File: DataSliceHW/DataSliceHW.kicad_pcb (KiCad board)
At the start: 2 copper layers, 85.5 x 54 mm, 119 parts, among them J1 Micro_SD_Card_Det2, Q1 BC847BDW1, SW1 SKRPABE010, SW10 SKRPABE010, SW11 SKRPABE010, SW12 SKRPABE010, SW13 SKRPABE010, SW14 SKRPABE010, SW15 SKRPABE010, SW16 SKRPABE010, SW17 SKRPABE010, SW18 SKRPABE010, SW19 SKRPABE010, SW2 SKRPABE010, SW20 SKRPABE010, SW21 SKRPABE010, SW22 SKRPABE010, SW23 SKRPABE010, SW24 SKRPABE010, SW25 SKRPABE010, SW26 SKRPABE010, SW27 SKRPABE010, SW28 SKRPABE010, SW29 SKRPABE010, SW3 SKRPABE010, SW30 SKRPABE010, SW31 SKRPABE010, SW32 SKRPABE010, SW33 SKRPABE010, SW34 SKRPABE010, SW35 SKRPABE010, SW36 SKRPABE010, SW37 SKRPABE010, SW38 SKRPABE010, SW39 SKRPABE010, SW4 SKRPABE010, SW40 SKRPABE010, SW41 SKRPABE010, SW42 SKRPABE010, SW43 SKRPABE010, SW44 SKRPABE010, SW45 SKRPABE010, SW46 SKRPABE010, SW47 SKRPABE010, SW48 SKRPABE010, SW49 SKRKAHE020, SW5 SKRPABE010, SW50 SKRKAHE020, SW6 SKRPABE010, SW7 SKRPABE010, SW8 SKRPABE010, SW9 SKRPABE010, U1 ESP32-S3-WROOM-1, U2 CP2102N-Axx-xQFN28

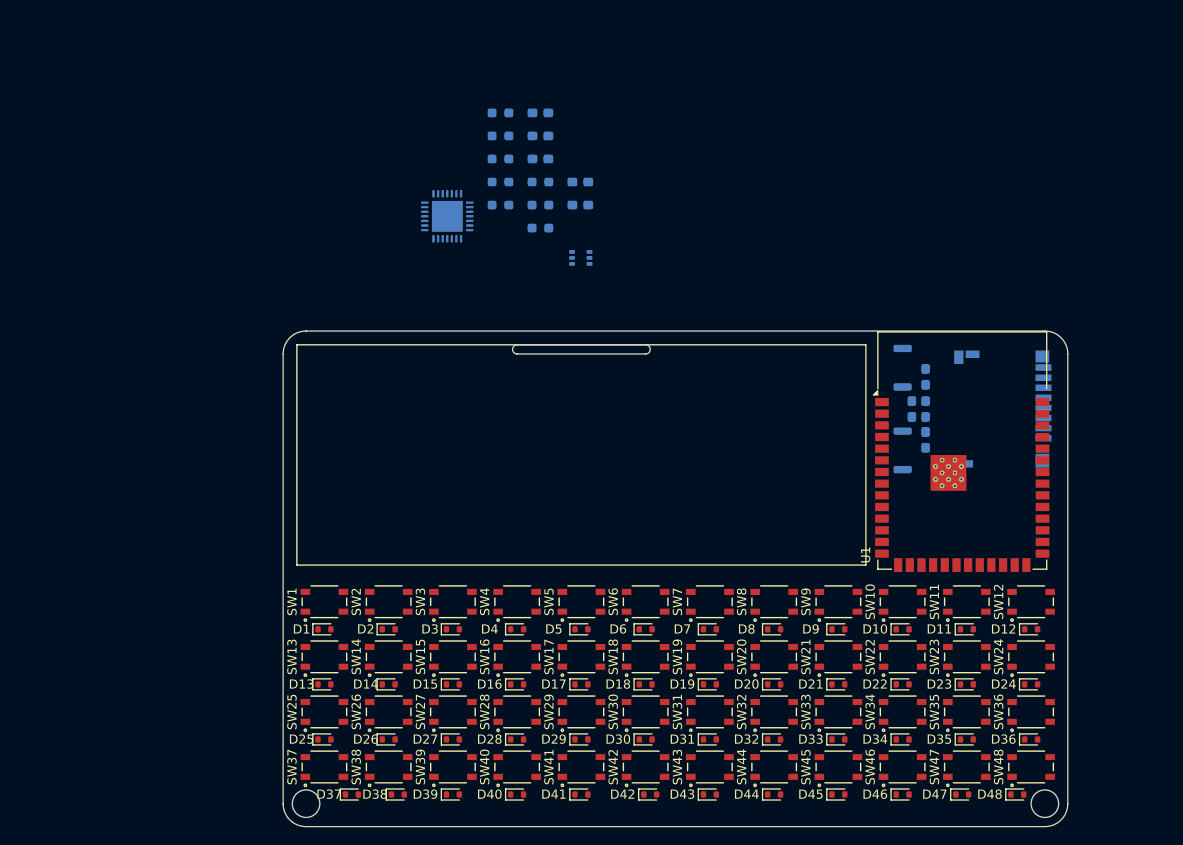
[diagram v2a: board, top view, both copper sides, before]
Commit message: Added OLED schematic
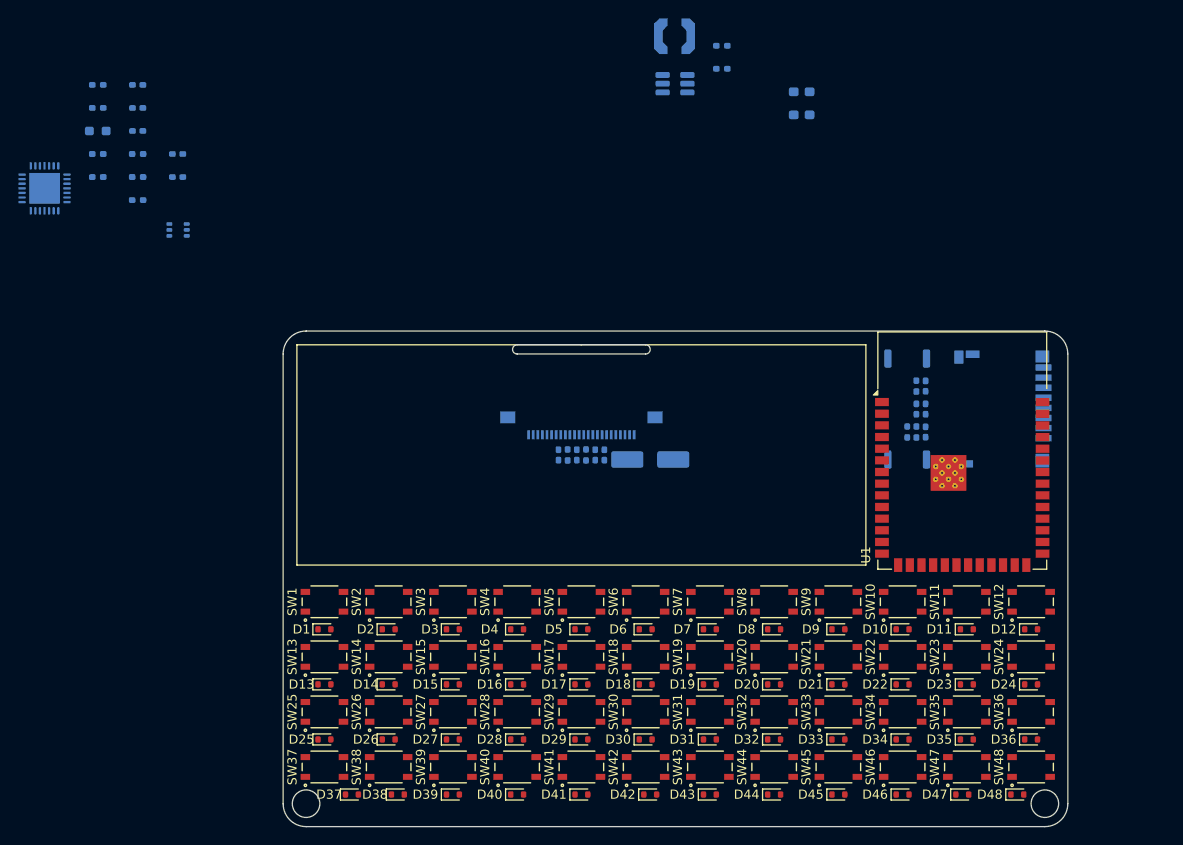
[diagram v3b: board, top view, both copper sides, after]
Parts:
- added C10: 22uF/50V(10%), Capacitor_SMD:C_0603_1608Metric_Pad1.08x0.95mm_HandSolder, B.Cu at (106.5, 23.9)
- added C11: 22uF/50V(10%), Capacitor_SMD:C_0603_1608Metric_Pad1.08x0.95mm_HandSolder, B.Cu at (106.5, 26.4)
- added C12: 4.7uF/50V(10%), Capacitor_SMD:C_0402_1005Metric_Pad0.74x0.62mm_HandSolder, B.Cu at (85.0, 63.5)
- added C5: 4.7uF/16V(10%), Capacitor_SMD:C_0402_1005Metric_Pad0.74x0.62mm_HandSolder, B.Cu at (80.0, 63.5)
- added C8: 100nF/16V(10%), Capacitor_SMD:C_0402_1005Metric_Pad0.74x0.62mm_HandSolder, B.Cu at (82.0, 63.5)
- added C9: 4.7uF/50V(10%), Capacitor_SMD:C_0402_1005Metric_Pad0.74x0.62mm_HandSolder, B.Cu at (84.0, 63.5)
- added D49: SS14, Diode_SMD:D_SMA_Handsoldering, B.Cu at (90.0, 64.0)
- added J2: 6871XX183622_687124183622, DataSlice:687124183622, B.Cu at (82.5, 59.0)
- added L1: 4.7uH, Inductor_SMD:L_Coilcraft_LPS4018, B.Cu at (92.7, 17.9)
- added R10: 200K(1%), Resistor_SMD:R_0402_1005Metric_Pad0.72x0.64mm_HandSolder, B.Cu at (97.8, 18.9)
- added R11: 10K(1%), Resistor_SMD:R_0402_1005Metric_Pad0.72x0.64mm_HandSolder, B.Cu at (97.8, 21.4)
- added R2: 10K(1%), Resistor_SMD:R_0402_1005Metric_Pad0.72x0.64mm_HandSolder, B.Cu at (119.0, 56.0)
- added R4: 10K(1%), Resistor_SMD:R_0402_1005Metric_Pad0.72x0.64mm_HandSolder, B.Cu at (81.0, 63.5)
- added R7: 4.7K(1%), Resistor_SMD:R_0402_1005Metric_Pad0.72x0.64mm_HandSolder, B.Cu at (119.0, 61.0)
- added R8: 4.7K(1%), Resistor_SMD:R_0402_1005Metric_Pad0.72x0.64mm_HandSolder, B.Cu at (118.0, 61.0)
- added R9: 1M(1%), Resistor_SMD:R_0402_1005Metric_Pad0.72x0.64mm_HandSolder, B.Cu at (83.0, 63.5)
- added U3: MT3608/SX1308, Package_TO_SOT_SMD:SOT-23-6_Handsoldering, B.Cu at (92.7, 23.1)
- C1, C2: footprint Capacitor_SMD:C_0603_1608Metric_Pad1.08x0.95mm_HandSolder -> Capacitor_SMD:C_0402_1005Metric_Pad0.74x0.62mm_HandSolder
- C13: renamed from C5; footprint Capacitor_SMD:C_0603_1608Metric_Pad1.08x0.95mm_HandSolder -> Capacitor_SMD:C_0402_1005Metric_Pad0.74x0.62mm_HandSolder
- C14: renamed from C6; footprint Capacitor_SMD:C_0603_1608Metric_Pad1.08x0.95mm_HandSolder -> Capacitor_SMD:C_0402_1005Metric_Pad0.74x0.62mm_HandSolder
- C15: renamed from C9; footprint Capacitor_SMD:C_0603_1608Metric_Pad1.08x0.95mm_HandSolder -> Capacitor_SMD:C_0402_1005Metric_Pad0.74x0.62mm_HandSolder
- C3: renamed from C7; footprint Capacitor_SMD:C_0603_1608Metric_Pad1.08x0.95mm_HandSolder -> Capacitor_SMD:C_0402_1005Metric_Pad0.74x0.62mm_HandSolder
- C4: renamed from C8; footprint Capacitor_SMD:C_0603_1608Metric_Pad1.08x0.95mm_HandSolder -> Capacitor_SMD:C_0402_1005Metric_Pad0.74x0.62mm_HandSolder
- C6: renamed from C3; footprint Capacitor_SMD:C_0603_1608Metric_Pad1.08x0.95mm_HandSolder -> Capacitor_SMD:C_0402_1005Metric_Pad0.74x0.62mm_HandSolder
- C7: renamed from C4; footprint Capacitor_SMD:C_0603_1608Metric_Pad1.08x0.95mm_HandSolder -> Capacitor_SMD:C_0402_1005Metric_Pad0.74x0.62mm_HandSolder
- R1: footprint Resistor_SMD:R_0603_1608Metric_Pad0.98x0.95mm_HandSolder -> Resistor_SMD:R_0402_1005Metric_Pad0.72x0.64mm_HandSolder
- R12: renamed from R4; footprint Resistor_SMD:R_0603_1608Metric_Pad0.98x0.95mm_HandSolder -> Resistor_SMD:R_0402_1005Metric_Pad0.72x0.64mm_HandSolder
- R13: renamed from R5; footprint Resistor_SMD:R_0603_1608Metric_Pad0.98x0.95mm_HandSolder -> Resistor_SMD:R_0402_1005Metric_Pad0.72x0.64mm_HandSolder
- R14: renamed from R7; footprint Resistor_SMD:R_0603_1608Metric_Pad0.98x0.95mm_HandSolder -> Resistor_SMD:R_0402_1005Metric_Pad0.72x0.64mm_HandSolder
- R15: renamed from R8; footprint Resistor_SMD:R_0603_1608Metric_Pad0.98x0.95mm_HandSolder -> Resistor_SMD:R_0402_1005Metric_Pad0.72x0.64mm_HandSolder
- R3: renamed from R2; footprint Resistor_SMD:R_0603_1608Metric_Pad0.98x0.95mm_HandSolder -> Resistor_SMD:R_0402_1005Metric_Pad0.72x0.64mm_HandSolder
- R5: renamed from R3; footprint Resistor_SMD:R_0603_1608Metric_Pad0.98x0.95mm_HandSolder -> Resistor_SMD:R_0402_1005Metric_Pad0.72x0.64mm_HandSolder
- moved C13 44.0 mm to (38.5, 33.2)
- moved C7 44.0 mm to (38.5, 30.7)
- moved Q1 44.0 mm to (38.5, 39.0)
- moved R12 44.0 mm to (29.8, 23.2)
- moved R13 44.0 mm to (29.8, 25.7)
- moved R14 44.0 mm to (29.8, 30.7)
- moved R15 44.0 mm to (29.8, 33.2)
- moved R6 44.0 mm to (29.8, 28.2)
- moved U2 44.0 mm to (24.0, 34.5)
- moved C15 44.0 mm to (34.1, 28.2)
- moved C3 44.0 mm to (34.1, 23.2)
- moved C4 44.0 mm to (34.1, 25.7)
- moved R1 44.0 mm to (34.1, 30.7)
- moved R3 44.0 mm to (34.1, 33.2)
- moved R5 44.0 mm to (34.1, 35.7)
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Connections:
- J1 pad 1: /SD_D2 -> unconnected-(J1-DAT2-Pad1)
- J1 pad 2: /SD_D3 -> Net-(J1-DAT3/CD)
- J1 pad 8: /SD_D1 -> unconnected-(J1-DAT1-Pad8)
- U1 pad 33: /SD_D1 -> unconnected-(U1-IO40-Pad33)
- U1 pad 34: /SD_D2 -> /I2C_SDA
- U1 pad 35: /SD_D3 -> /I2C_SCL

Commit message: Schematic and board progress
Updated gitignore and removed some ignored files
Added power schematic with battery chagrer
Some adjustments to components
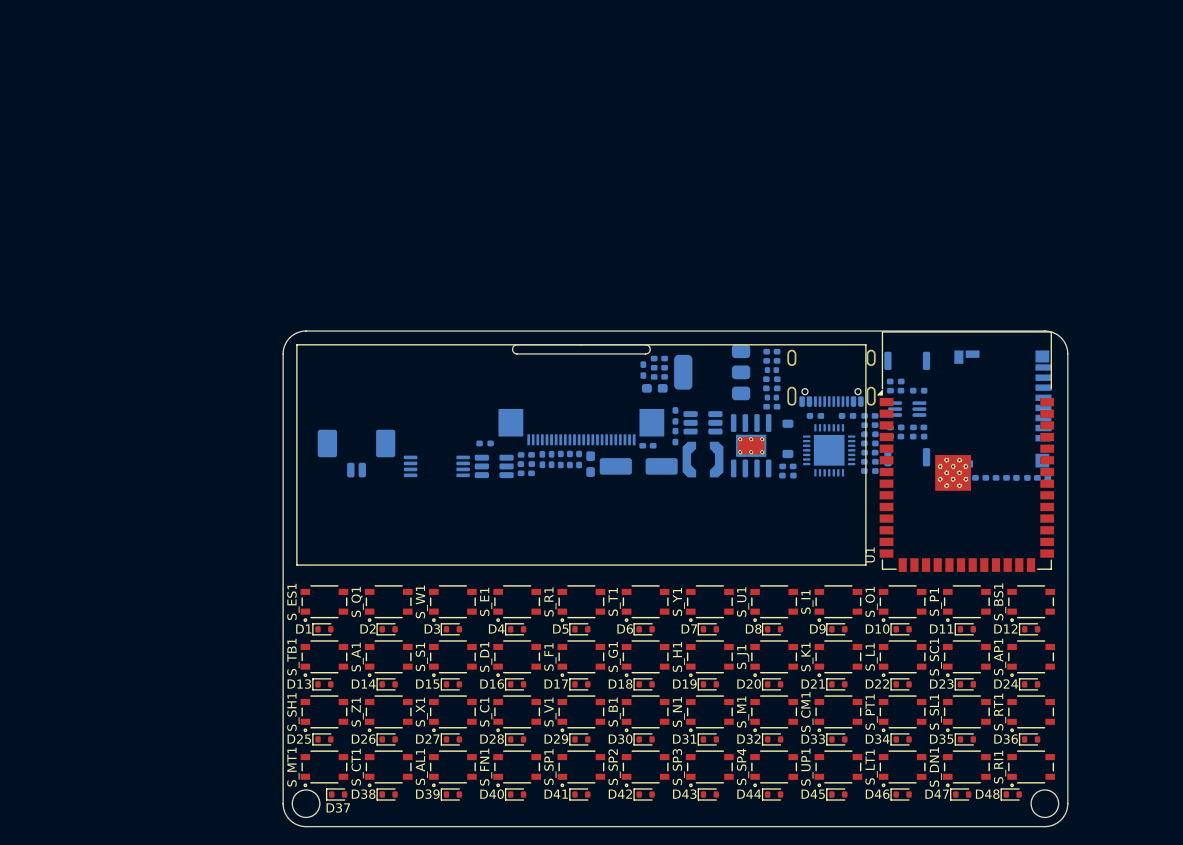
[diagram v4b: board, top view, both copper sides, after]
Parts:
- removed SW1, SW10, SW11, SW12, SW13, SW14, SW15, SW16, SW17, SW18, SW19, SW2, SW20, SW21, SW22, SW23, SW24, SW25, SW26, SW27, SW28, SW29, SW3, SW30, SW31, SW32, SW33, SW34, SW35, SW36, SW37, SW38, SW39, SW4, SW40, SW41, SW42, SW43, SW44, SW45, SW46, SW47, SW48, SW5, SW6, SW7, SW8, SW9: SKRPABE010, DataSlice:SW4_SKRPABE010_ALPS
- added C10: 10uF/25V(20%), Capacitor_SMD:C_0402_1005Metric_Pad0.74x0.62mm_HandSolder, B.Cu at (103.2, 53.2)
- added C11: 0.1uF/50V(10%), Capacitor_SMD:C_0402_1005Metric_Pad0.74x0.62mm_HandSolder, B.Cu at (103.2, 52.2)
- added C12: 0.1uF/50V(10%), Capacitor_SMD:C_0402_1005Metric_Pad0.74x0.62mm_HandSolder, B.Cu at (91.0, 55.0)
- added C13: 10uF/25V(20%), Capacitor_SMD:C_0402_1005Metric_Pad0.74x0.62mm_HandSolder, B.Cu at (91.0, 54.0)
- added C15: 10uF/25V(20%), Capacitor_SMD:C_0402_1005Metric_Pad0.74x0.62mm_HandSolder, B.Cu at (76.5, 63.5)
- added C17: 0.1uF/50V(10%), Capacitor_SMD:C_0402_1005Metric_Pad0.74x0.62mm_HandSolder, B.Cu at (76.5, 65.5)
- added C18: 0.1uF/50V(10%), Capacitor_SMD:C_0402_1005Metric_Pad0.74x0.62mm_HandSolder, B.Cu at (103.2, 58.2)
- added C4: 10uF/25V(20%), Capacitor_SMD:C_0402_1005Metric_Pad0.74x0.62mm_HandSolder, B.Cu at (105.0, 64.8)
- added D49: 1N5819HW-7-F, Diode_SMD:D_SOD-123, B.Cu at (105.0, 61.8)
- added D50: RED, LED_SMD:LED_0402_1005Metric, B.Cu at (103.2, 54.2)
- added D51: RED, LED_SMD:LED_0402_1005Metric, B.Cu at (103.2, 57.2)
- added J1: USB4105-GF-A, Connector_USB:USB_C_Receptacle_GCT_USB4105-xx-A_16P_TopMnt_Horizontal, B.Cu at (109.8, 54.0)
- added J4: 53261-0271, Connector_Molex:Molex_PicoBlade_53261-0271_1x02-1MP_P1.25mm_Horizontal, B.Cu at (58.0, 62.8)
- added Q2: FS8205A, Package_SO:TSSOP-8_4.4x3mm_P0.65mm, B.Cu at (66.8, 64.8)
- added R14: 100R(1%), Resistor_SMD:R_0402_1005Metric_Pad0.72x0.64mm_HandSolder, B.Cu at (76.5, 64.5)
- added R15: 1K(1%), Resistor_SMD:R_0402_1005Metric_Pad0.72x0.64mm_HandSolder, B.Cu at (103.2, 56.2)
- added R16: 1K(1%), Resistor_SMD:R_0402_1005Metric_Pad0.72x0.64mm_HandSolder, B.Cu at (72.0, 62.2)
- added R17: 1K(1%), Resistor_SMD:R_0402_1005Metric_Pad0.72x0.64mm_HandSolder, B.Cu at (103.2, 55.2)
- added R18: 3K(1%), Resistor_SMD:R_0402_1005Metric_Pad0.72x0.64mm_HandSolder, B.Cu at (105.0, 65.8)
- added R5: 5.1K(1%), Resistor_SMD:R_0402_1005Metric_Pad0.72x0.64mm_HandSolder, B.Cu at (108.0, 59.2)
- added R6: 5.1K(1%), Resistor_SMD:R_0402_1005Metric_Pad0.72x0.64mm_HandSolder, B.Cu at (111.5, 59.2)
- added S_A1: SKRPABE010, DataSlice:SW4_SKRPABE010_ALPS, F.Cu at (61.5, 85.5)
- added S_AL1: SKRPABE010, DataSlice:SW4_SKRPABE010_ALPS, F.Cu at (68.5, 97.5)
- added S_AP1: SKRPABE010, DataSlice:SW4_SKRPABE010_ALPS, F.Cu at (131.5, 85.5)
- added S_B1: SKRPABE010, DataSlice:SW4_SKRPABE010_ALPS, F.Cu at (89.5, 91.5)
- added S_BS1: SKRPABE010, DataSlice:SW4_SKRPABE010_ALPS, F.Cu at (131.5, 79.5)
- added S_C1: SKRPABE010, DataSlice:SW4_SKRPABE010_ALPS, F.Cu at (75.5, 91.5)
- added S_CM1: SKRPABE010, DataSlice:SW4_SKRPABE010_ALPS, F.Cu at (110.5, 91.5)
- added S_CT1: SKRPABE010, DataSlice:SW4_SKRPABE010_ALPS, F.Cu at (61.5, 97.5)
- added S_D1: SKRPABE010, DataSlice:SW4_SKRPABE010_ALPS, F.Cu at (75.5, 85.5)
- added S_DN1: SKRPABE010, DataSlice:SW4_SKRPABE010_ALPS, F.Cu at (124.5, 97.5)
- added S_E1: SKRPABE010, DataSlice:SW4_SKRPABE010_ALPS, F.Cu at (75.5, 79.5)
- added S_ES1: SKRPABE010, DataSlice:SW4_SKRPABE010_ALPS, F.Cu at (54.5, 79.5)
- added S_F1: SKRPABE010, DataSlice:SW4_SKRPABE010_ALPS, F.Cu at (82.5, 85.5)
- added S_FN1: SKRPABE010, DataSlice:SW4_SKRPABE010_ALPS, F.Cu at (75.5, 97.5)
- added S_G1: SKRPABE010, DataSlice:SW4_SKRPABE010_ALPS, F.Cu at (89.5, 85.5)
- added S_H1: SKRPABE010, DataSlice:SW4_SKRPABE010_ALPS, F.Cu at (96.5, 85.5)
- added S_I1: SKRPABE010, DataSlice:SW4_SKRPABE010_ALPS, F.Cu at (110.5, 79.5)
- added S_J1: SKRPABE010, DataSlice:SW4_SKRPABE010_ALPS, F.Cu at (103.5, 85.5)
- added S_K1: SKRPABE010, DataSlice:SW4_SKRPABE010_ALPS, F.Cu at (110.5, 85.5)
- added S_L1: SKRPABE010, DataSlice:SW4_SKRPABE010_ALPS, F.Cu at (117.5, 85.5)
- added S_LT1: SKRPABE010, DataSlice:SW4_SKRPABE010_ALPS, F.Cu at (117.5, 97.5)
- added S_M1: SKRPABE010, DataSlice:SW4_SKRPABE010_ALPS, F.Cu at (103.5, 91.5)
- added S_MT1: SKRPABE010, DataSlice:SW4_SKRPABE010_ALPS, F.Cu at (54.5, 97.5)
- added S_N1: SKRPABE010, DataSlice:SW4_SKRPABE010_ALPS, F.Cu at (96.5, 91.5)
- added S_O1: SKRPABE010, DataSlice:SW4_SKRPABE010_ALPS, F.Cu at (117.5, 79.5)
- added S_P1: SKRPABE010, DataSlice:SW4_SKRPABE010_ALPS, F.Cu at (124.5, 79.5)
- added S_PT1: SKRPABE010, DataSlice:SW4_SKRPABE010_ALPS, F.Cu at (117.5, 91.5)
- added S_Q1: SKRPABE010, DataSlice:SW4_SKRPABE010_ALPS, F.Cu at (61.5, 79.5)
- added S_R1: SKRPABE010, DataSlice:SW4_SKRPABE010_ALPS, F.Cu at (82.5, 79.5)
- added S_RI1: SKRPABE010, DataSlice:SW4_SKRPABE010_ALPS, F.Cu at (131.5, 97.5)
- added S_RT1: SKRPABE010, DataSlice:SW4_SKRPABE010_ALPS, F.Cu at (131.5, 91.5)
- added S_S1: SKRPABE010, DataSlice:SW4_SKRPABE010_ALPS, F.Cu at (68.5, 85.5)
- added S_SC1: SKRPABE010, DataSlice:SW4_SKRPABE010_ALPS, F.Cu at (124.5, 85.5)
- added S_SH1: SKRPABE010, DataSlice:SW4_SKRPABE010_ALPS, F.Cu at (54.5, 91.5)
- added S_SL1: SKRPABE010, DataSlice:SW4_SKRPABE010_ALPS, F.Cu at (124.5, 91.5)
- added S_SP1: SKRPABE010, DataSlice:SW4_SKRPABE010_ALPS, F.Cu at (82.5, 97.5)
- added S_SP2: SKRPABE010, DataSlice:SW4_SKRPABE010_ALPS, F.Cu at (89.5, 97.5)
- added S_SP3: SKRPABE010, DataSlice:SW4_SKRPABE010_ALPS, F.Cu at (96.5, 97.5)
- added S_SP4: SKRPABE010, DataSlice:SW4_SKRPABE010_ALPS, F.Cu at (103.5, 97.5)
- added S_T1: SKRPABE010, DataSlice:SW4_SKRPABE010_ALPS, F.Cu at (89.5, 79.5)
- added S_TB1: SKRPABE010, DataSlice:SW4_SKRPABE010_ALPS, F.Cu at (54.5, 85.5)
- added S_U1: SKRPABE010, DataSlice:SW4_SKRPABE010_ALPS, F.Cu at (103.5, 79.5)
- added S_UP1: SKRPABE010, DataSlice:SW4_SKRPABE010_ALPS, F.Cu at (110.5, 97.5)
- added S_V1: SKRPABE010, DataSlice:SW4_SKRPABE010_ALPS, F.Cu at (82.5, 91.5)
- added S_W1: SKRPABE010, DataSlice:SW4_SKRPABE010_ALPS, F.Cu at (68.5, 79.5)
- added S_X1: SKRPABE010, DataSlice:SW4_SKRPABE010_ALPS, F.Cu at (68.5, 91.5)
- added S_Y1: SKRPABE010, DataSlice:SW4_SKRPABE010_ALPS, F.Cu at (96.5, 79.5)
- added S_Z1: SKRPABE010, DataSlice:SW4_SKRPABE010_ALPS, F.Cu at (61.5, 91.5)
- added U3: AMS1117-3.3 / SGM2212-3.3, Package_TO_SOT_SMD:SOT-223-3_TabPin2, B.Cu at (96.8, 54.5)
- added U4: DW01A, Package_TO_SOT_SMD:SOT-23-6_Handsoldering, B.Cu at (73.0, 64.8)
- added U5: TP4056-42-ESOP8, Package_SO:SOIC-8-1EP_3.9x4.9mm_P1.27mm_EP2.41x3.3mm_ThermalVias, B.Cu at (101.0, 62.5)
- C16: renamed from C8; value 100nF/16V(10%) -> 0.1uF/50V(10%)
- C2: renamed from C1; value 10uF/16V(10%) -> 10uF/25V(20%)
- C21: renamed from C6; value 100nF/16V(10%) -> 0.1uF/50V(10%)
- C3: value 10uF/16V(10%) -> 10uF/25V(20%)
- C6: renamed from C2; value 100nF/16V(10%) -> 0.1uF/50V(10%)
- C9: renamed from C4; value 100nF/16V(10%) -> 0.1uF/50V(10%)
- J2: value 6871XX183622_687124183622 -> 68712414522; footprint DataSlice:687124183622 -> DataSlice:68712414522
- J3: renamed from J1; value Micro_SD_Card_Det2 -> DM3D-SF
- Q1: footprint Package_TO_SOT_SMD:SOT-363_SC-70-6 -> Package_TO_SOT_SMD:SOT-363_SC-70-6_Handsoldering
- R10: renamed from R6; footprint Resistor_SMD:R_0603_1608Metric_Pad0.98x0.95mm_HandSolder -> Resistor_SMD:R_0402_1005Metric_Pad0.72x0.64mm_HandSolder
- U2: value CP2102N-Axx-xQFN28 -> CP2102N-A02-GQFN28
- moved R2 96.4 mm to (119.2, 61.5)
- moved R1 92.8 mm to (116.8, 55.5), turned to 0 degrees
- moved R7 92.4 mm to (119.2, 56.5), turned to 0 degrees
- moved R10 91.9 mm to (113.9, 65.2), turned to 0 degrees
- moved R3 91.9 mm to (116.8, 60.5)
- moved C7 91.0 mm to (119.2, 60.5), turned to 0 degrees
- moved U2 90.1 mm to (109.5, 63.0), turned to -90 degrees
- moved C3 88.0 mm to (113.9, 60.2)
- moved C9 86.6 mm to (113.9, 59.2), turned to 0 degrees
- moved R4 86.5 mm to (113.9, 64.2)
- moved R8 84.6 mm to (113.9, 61.2)
- moved R9 84.1 mm to (113.9, 62.2), turned to 0 degrees
- moved C8 82.2 mm to (113.9, 63.2), turned to 0 degrees
- moved Q1 81.8 mm to (118.0, 58.5)
- moved C1 81.6 mm to (116.8, 56.5)
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- renumbered C13 to C1, C5 to C14, C9 to C19, C12 to C20, C10 to C22, C11 to C23, C14 to C5, C15 to C7, C7 to C8, D49 to D52, R12 to R1, R7 to R11, R8 to R12, R4 to R13, R9 to R19, R13 to R2, R2 to R20, R10 to R21, R11 to R22, R14 to R3, R1 to R4, R15 to R7, R3 to R8, R5 to R9, SW49 to S_PR1, SW50 to S_RS1, U3 to U6

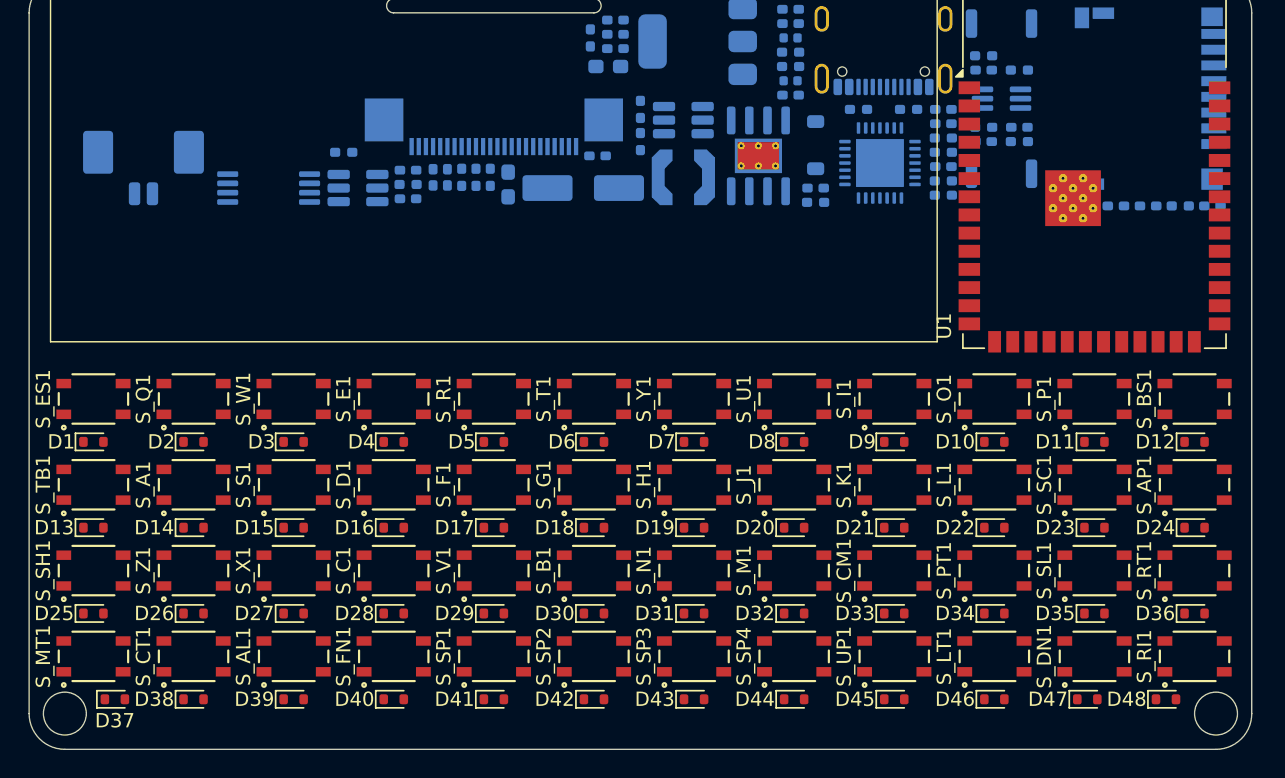
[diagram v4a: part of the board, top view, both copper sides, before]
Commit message: Board adjustments and some renders
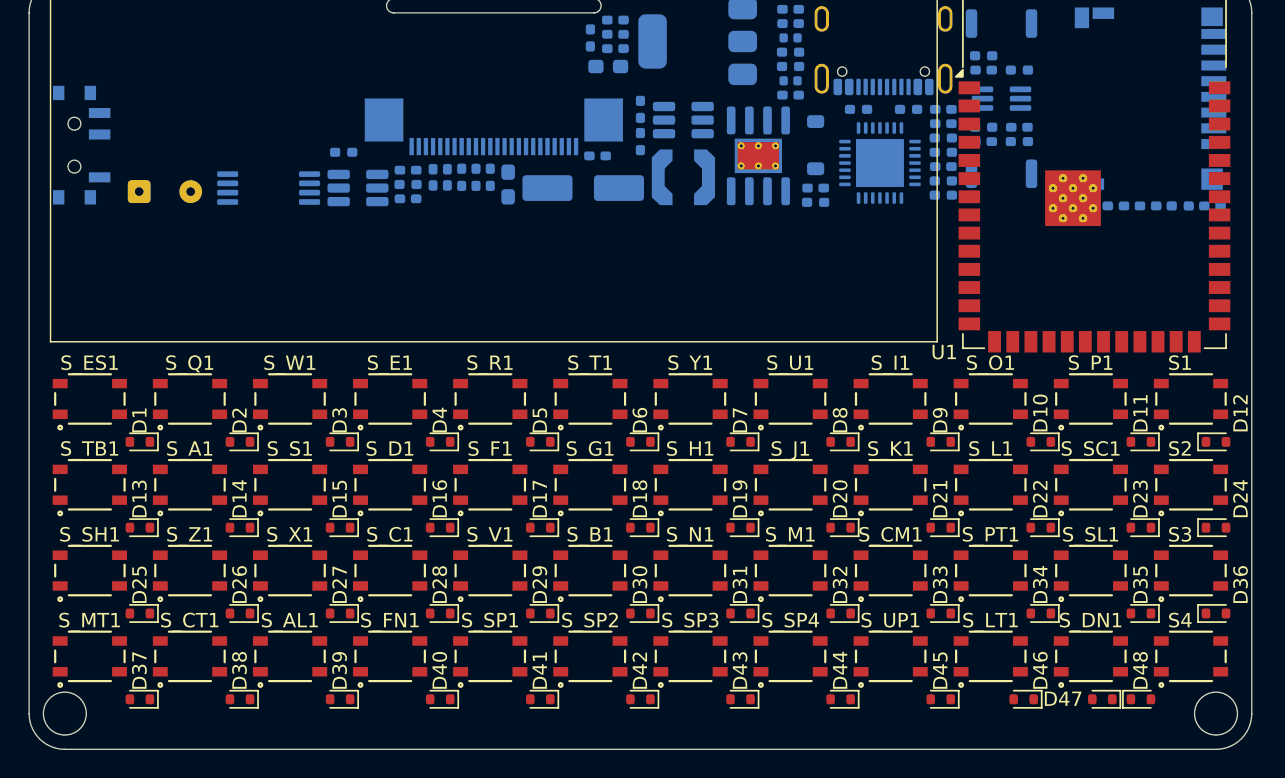
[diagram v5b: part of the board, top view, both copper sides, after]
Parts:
- added SW1: K3-1391D-5MM, Button_Switch_SMD:SW_SPDT_PCM12, B.Cu at (53.5, 61.8)
- J3: renamed from J4; footprint Connector_Molex:Molex_PicoBlade_53261-0271_1x02-1MP_P1.25mm_Horizontal -> Connector_Wire:SolderWire-0.1sqmm_1x02_P3.6mm_D0.4mm_OD1mm
- moved D1 3.25 mm to (57.8, 82.5), turned to 180 degrees
- moved D10 3.25 mm to (120.8, 82.5), turned to 180 degrees
- moved D11 3.25 mm to (127.8, 82.5), turned to 180 degrees
- moved D13 3.25 mm to (57.8, 88.5), turned to 180 degrees
- moved D14 3.25 mm to (64.8, 88.5), turned to 180 degrees
- moved D15 3.25 mm to (71.8, 88.5), turned to 180 degrees
- moved D16 3.25 mm to (78.8, 88.5), turned to 180 degrees
- moved D17 3.25 mm to (85.8, 88.5), turned to 180 degrees
- moved D18 3.25 mm to (92.8, 88.5), turned to 180 degrees
- moved D19 3.25 mm to (99.8, 88.5), turned to 180 degrees
- moved D2 3.25 mm to (64.8, 82.5), turned to 180 degrees
- moved D20 3.25 mm to (106.8, 88.5), turned to 180 degrees
- moved D21 3.25 mm to (113.8, 88.5), turned to 180 degrees
- moved D22 3.25 mm to (120.8, 88.5), turned to 180 degrees
- moved D23 3.25 mm to (127.8, 88.5), turned to 180 degrees
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- renumbered J3 to J4, S_BS1 to S1, S_AP1 to S2, S_RT1 to S3, S_RI1 to S4
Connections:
- J3 pad 1: +4V -> Net-(J3-Pin_1)
